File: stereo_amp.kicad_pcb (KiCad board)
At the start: 2 copper layers, 125 x 94 mm, 122 parts, among them J101 HEADER1X2, J102 HEADER1X2, J103 HEADER1X2, J104 HEADER1X2, J105 HEADER1X3, J106 VCCL, J107 VCCR, J108 HEADER1X3, J109 HEADER1X2, J110 HEADER1X2, J111 HEADER1X3, J112 HEADER1X3, Q201 BC309B, Q202 BC237B, Q203 BD135, Q204 BD136, Q205 BD243C, Q206 BD244C, Q301 BC309B, Q302 BC237B, Q303 BD135, Q304 BD136, Q305 BD243C, Q306 BD244C

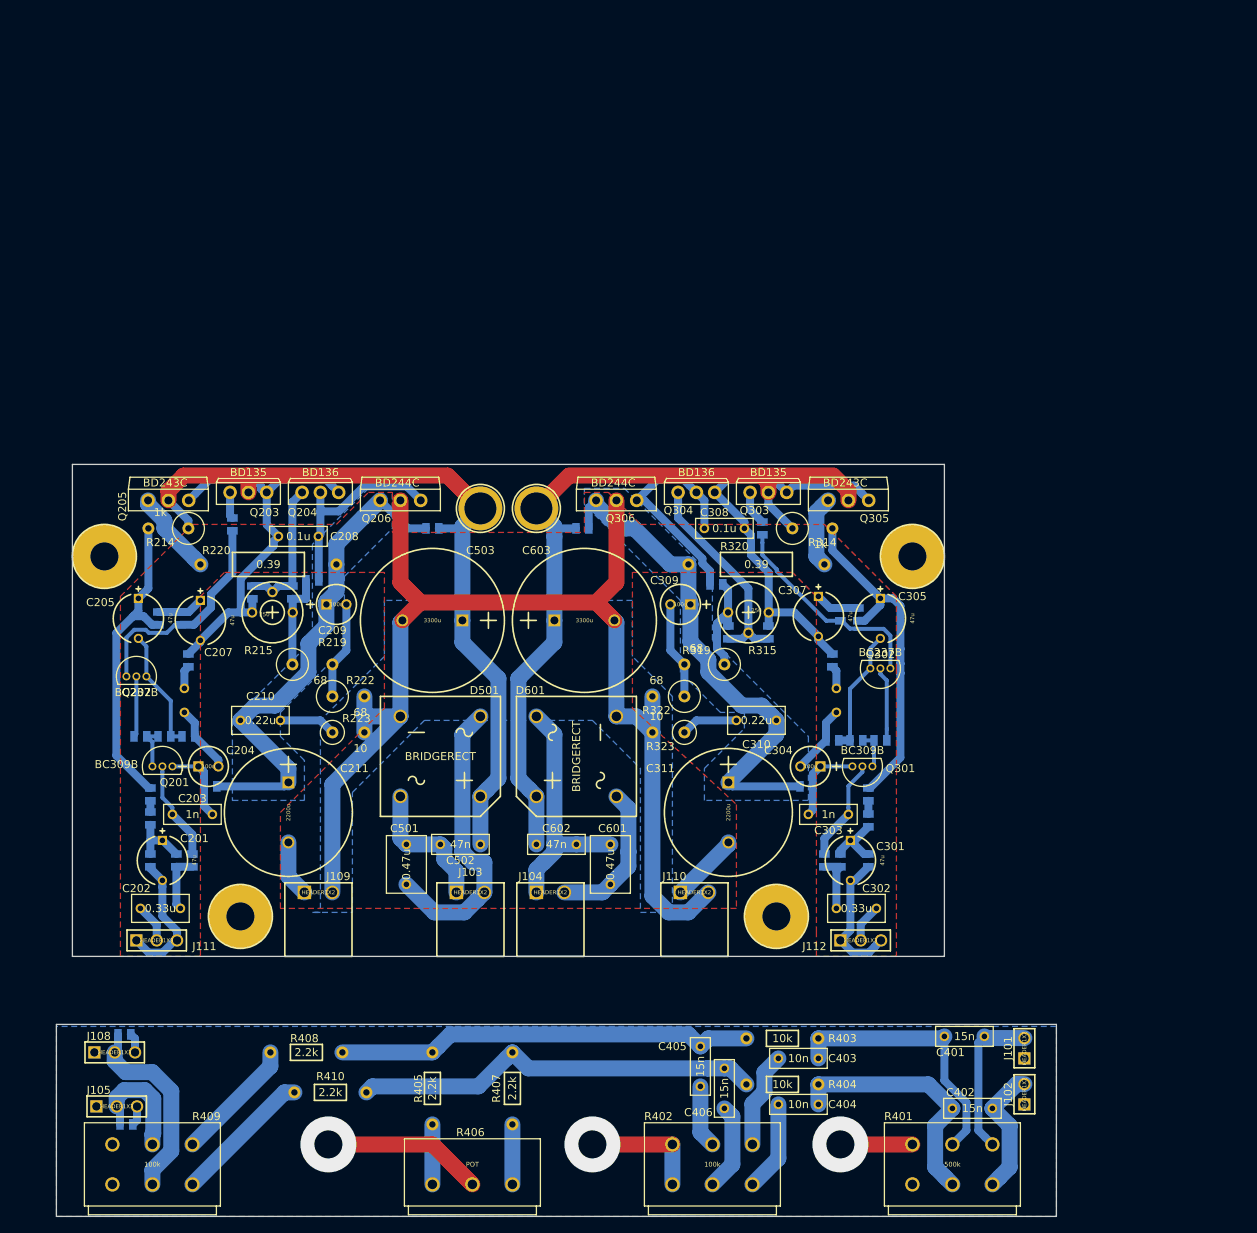
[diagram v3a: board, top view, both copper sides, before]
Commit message: Turned all power transistors around. Resized filter board to fit knobs.
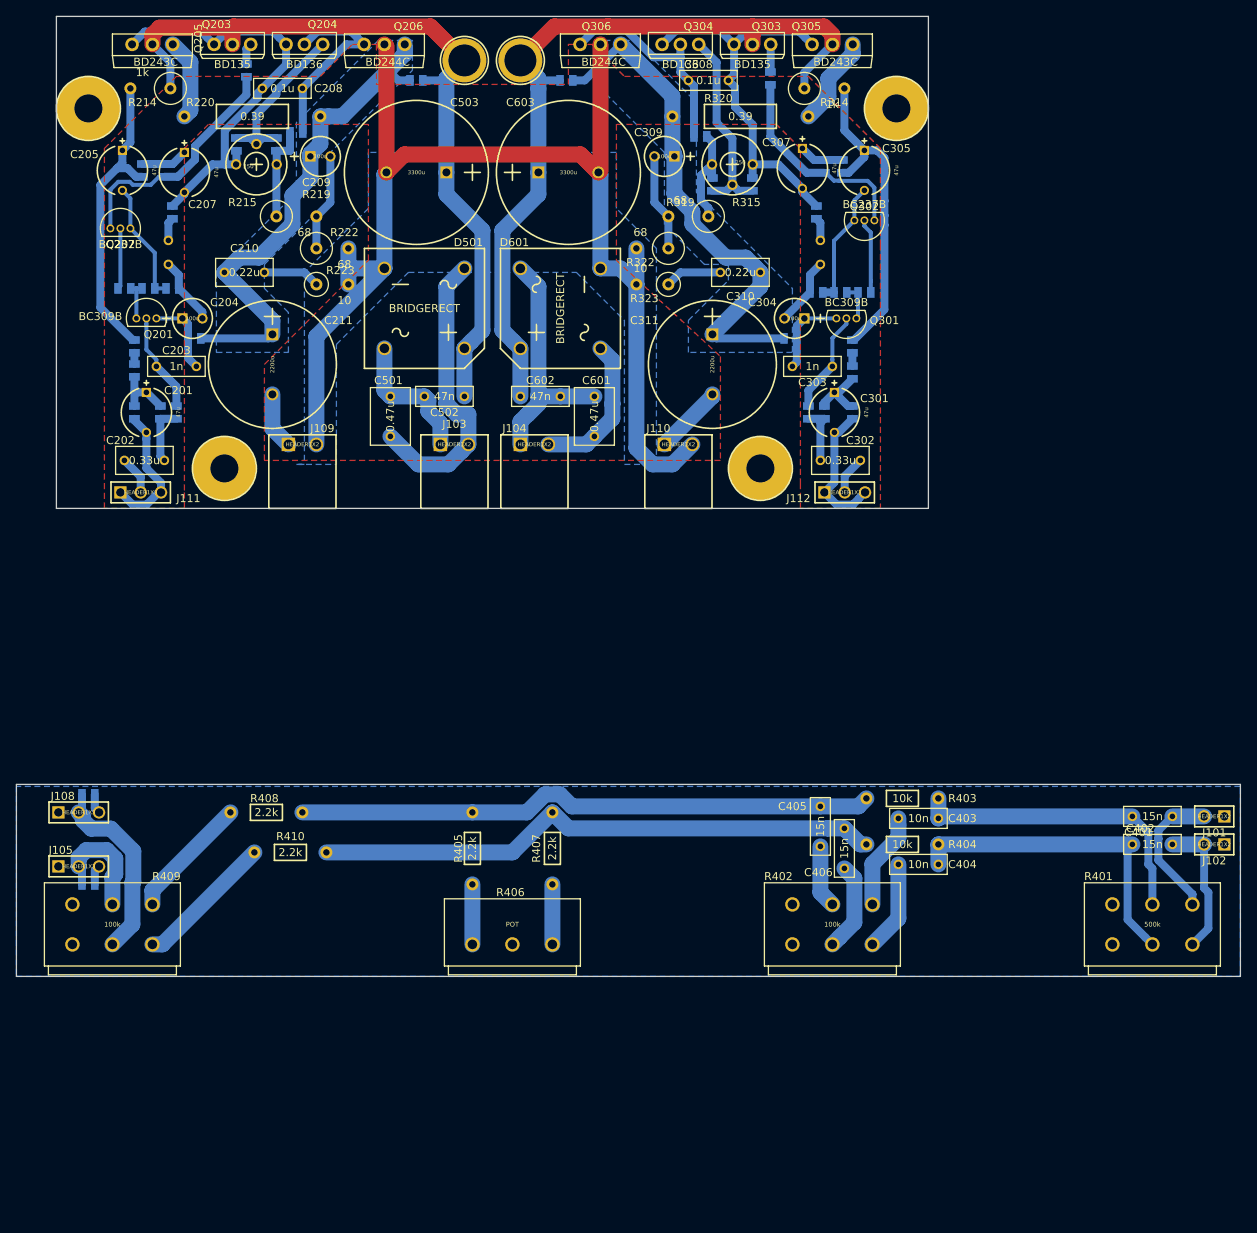
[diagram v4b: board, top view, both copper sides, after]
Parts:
- removed the MountHole_D35P80 at (56.0, 126.5)
- removed the MountHole_D35P80 at (123.0, 126.5)
- removed the MountHole_D35P80 at (39.0, 81.5)
- added MountHole_D35P80: VAL**, Newlib:MountHole_D35P80, F.Cu at (54.0, 70.5)
- added MountHole_D35P80: VAL**, Newlib:MountHole_D35P80, F.Cu at (121.0, 70.5)
- added MountHole_D35P80: VAL**, Newlib:MountHole_D35P80, F.Cu at (37.0, 25.5)
- moved Q205 57.0 mm to (45.0, 17.5), turned to 0 degrees
- moved Q206 57.0 mm to (74.0, 17.5), turned to 0 degrees
- moved Q305 57.0 mm to (130.0, 17.5), turned to 0 degrees
- moved Q306 57.0 mm to (101.0, 17.5), turned to 0 degrees
- moved R213 56.8 mm to (56.8, 20.8)
- moved R313 56.3 mm to (122.2, 21.8)
- moved C201 56.0 mm to (44.2, 63.5)
- moved C202 56.0 mm to (44.0, 69.5)
- moved C203 56.0 mm to (48.0, 57.8)
- moved C204 56.0 mm to (50.0, 51.8)
- moved C205 56.0 mm to (41.2, 33.2)
- moved C206 56.0 mm to (47.0, 43.5)
- moved C207 56.0 mm to (49.0, 33.5)
- moved C208 56.0 mm to (61.2, 23.0)
- moved C209 56.0 mm to (66.0, 31.5)
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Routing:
- net GND: track 268.2 -> 228.7 mm, vias 3 -> 0
- net Net-(C405-Pad1): track 52.5 -> 72.5 mm
- net Net-(C406-Pad2): track 51.2 -> 71.2 mm
- net Net-(C402-Pad2): track 31.8 -> 40.8 mm
- net Net-(C401-Pad2): track 33.7 -> 38.9 mm
- net Net-(Q204-Pad3): track 17.8 -> 21.5 mm
- net Net-(C305-Pad1): track 43.1 -> 40.6 mm
- net Net-(Q202-Pad1): track 28.0 -> 30.3 mm
- net Net-(Q305-Pad3): track 9.02 -> 11.3 mm
- net /Filters/IN_L: track 19.6 -> 17.4 mm
- net Net-(C308-Pad2): track 29.0 -> 26.9 mm
- net Net-(Q304-Pad3): track 26.8 -> 24.9 mm
- net /Power Supply Left/OUT: track 101.3 -> 102.9 mm
- net Net-(C307-Pad2): track 51.6 -> 50.2 mm
- net Net-(C208-Pad2): track 25.7 -> 24.3 mm
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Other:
- board size 125 x 94 mm -> 153 x 120 mm
